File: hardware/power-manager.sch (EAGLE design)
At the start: 77 parts, among them IC1 ATMEGA168-AU, K1 G6J-2FL-Y, K2 G6J-2FL-Y, K3 G6J-2FL-Y, Q1 BSS138, Q2 BSS138, Q3 BSS138, U1 V_REG_LDOSMD, U2 INA219, U3 TPS2552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

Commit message: hw: rc2
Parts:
- added C20, C21, C22, C23: .1u, rcl:C-EUC0805
- added LED7: (no value), led:LEDSML0805
- added R24, R25, R26, R27, R28, R29: 10k, rcl:R-EU_R0603
- added R30: 330, rcl:R-EU_R0603
- added R31: 100k, rcl:R-EU_R0603
- U1: value V_REG_LDOSMD -> MIC5301
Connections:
- removed net LED_SYS: IC1.PC0(ADC0/PCINT8), R20.1
- removed net N$21: K12.P, K13.P, X2.1.SK
- new net POWER_ADC: C22.1, IC1.PC0(ADC0/PCINT8), R28.2, R29.1
- new net POWER_IN: K12.P, K13.P, R28.1, X2.1.SK
- new net USB1_ADC: C20.1, IC1.ADC7, R24.2, R25.1
- new net USB1_IN: C9.1, JP1.1, R24.1, U$2.VBUS, U3.IN
- new net USB2_ADC: C21.1, IC1.ADC6, R26.2, R27.1
- new net USB2_IN: C11.1, R26.1, U$3.VBUS, U7.IN
- net GND: now also C20.2, C21.2, C22.2, C23.2, LED7.C, R25.2, R27.2, R29.2, R31.2
- net MISO: now also R20.1
- net N$10: now also LED7.A, R30.2; no longer C11.1, U$3.VBUS, U7.IN
- net N$19: now also R31.1
- net N$5: now also C23.1, U1.BP; no longer C9.1, JP1.1, U$2.VBUS, U3.IN
- net SCK: now also R30.1
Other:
- note added: "Input Measurement"
- moved on the sheet: C1, C13, C18, C19, C2, ISP1, K1, LED1, LED2, LED3, LED4, LED5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

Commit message: hw: rc3
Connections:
- net POWER_ADC: now also IC1.ADC6; no longer IC1.PC0(ADC0/PCINT8)
- net USB1_ADC: now also IC1.PC0(ADC0/PCINT8); no longer IC1.ADC7
- net USB2_ADC: now also IC1.ADC7; no longer IC1.ADC6
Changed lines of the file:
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@@
 </segment>
 <segment>
-<pinref part="IC1" gate="1" pin="PC0(ADC0/PCINT8)"/>
-<wire x1="236.22" y1="243.84" x2="256.54" y2="243.84" width="0.1524" layer="91"/>
-<label x="256.54" y="243.84" size="1.778" layer="95" rot="MR0"/>
+<pinref part="IC1" gate="1" pin="ADC6"/>
+<wire x1="236.22" y1="228.6" x2="256.54" y2="228.6" width="0.1524" layer="91"/>
+<label x="256.54" y="228.6" size="1.778" layer="95" rot="MR0"/>
 </segment>
 </net>
@@
 </segment>
 <segment>
-<pinref part="IC1" gate="1" pin="ADC7"/>
-<wire x1="236.22" y1="226.06" x2="256.54" y2="226.06" width="0.1524" layer="91"/>
-<label x="256.54" y="226.06" size="1.778" layer="95" rot="MR0"/>
+<pinref part="IC1" gate="1" pin="PC0(ADC0/PCINT8)"/>
+<wire x1="236.22" y1="243.84" x2="256.54" y2="243.84" width="0.1524" layer="91"/>
+<label x="256.54" y="243.84" size="1.778" layer="95" rot="MR0"/>
 </segment>
 </net>
@@
 </segment>
 <segment>
-<pinref part="IC1" gate="1" pin="ADC6"/>
-<wire x1="236.22" y1="228.6" x2="256.54" y2="228.6" width="0.1524" layer="91"/>
-<label x="256.54" y="228.6" size="1.778" layer="95" rot="MR0"/>
+<pinref part="IC1" gate="1" pin="ADC7"/>
+<wire x1="236.22" y1="226.06" x2="256.54" y2="226.06" width="0.1524" layer="91"/>
+<label x="256.54" y="226.06" size="1.778" layer="95" rot="MR0"/>
 </segment>
 </net>

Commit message: hw: rc7
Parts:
- R24, R26: value 10k -> 56k
- R28: value 10k -> 270k
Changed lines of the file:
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@@
 <part name="GND48" library="supply1" deviceset="GND" device=""/>
 <part name="P+8" library="supply1" deviceset="+5V" device=""/>
-<part name="R24" library="rcl" deviceset="R-EU_" device="R0603" value="10k"/>
+<part name="R24" library="rcl" deviceset="R-EU_" device="R0603" value="56k"/>
 <part name="R25" library="rcl" deviceset="R-EU_" device="R0603" value="10k"/>
 <part name="C20" library="rcl" deviceset="C-EU" device="C0805" value=".1u"/>
 <part name="GND49" library="supply1" deviceset="GND" device=""/>
-<part name="R26" library="rcl" deviceset="R-EU_" device="R0603" value="10k"/>
+<part name="R26" library="rcl" deviceset="R-EU_" device="R0603" value="56k"/>
 <part name="R27" library="rcl" deviceset="R-EU_" device="R0603" value="10k"/>
 <part name="C21" library="rcl" deviceset="C-EU" device="C0805" value=".1u"/>
 <part name="GND50" library="supply1" deviceset="GND" device=""/>
-<part name="R28" library="rcl" deviceset="R-EU_" device="R0603" value="10k"/>
+<part name="R28" library="rcl" deviceset="R-EU_" device="R0603" value="270k"/>
 <part name="R29" library="rcl" deviceset="R-EU_" device="R0603" value="10k"/>
 <part name="C22" library="rcl" deviceset="C-EU" device="C0805" value=".1u"/>

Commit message: hw: rc8
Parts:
- R24, R26: value 56k -> 33k
- R25, R27, R29: value 10k -> 5k6
- R28: value 270k -> 180k
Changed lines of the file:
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@@
 <part name="GND48" library="supply1" deviceset="GND" device=""/>
 <part name="P+8" library="supply1" deviceset="+5V" device=""/>
-<part name="R24" library="rcl" deviceset="R-EU_" device="R0603" value="56k"/>
-<part name="R25" library="rcl" deviceset="R-EU_" device="R0603" value="10k"/>
+<part name="R24" library="rcl" deviceset="R-EU_" device="R0603" value="33k"/>
+<part name="R25" library="rcl" deviceset="R-EU_" device="R0603" value="5k6"/>
 <part name="C20" library="rcl" deviceset="C-EU" device="C0805" value=".1u"/>
 <part name="GND49" library="supply1" deviceset="GND" device=""/>
-<part name="R26" library="rcl" deviceset="R-EU_" device="R0603" value="56k"/>
-<part name="R27" library="rcl" deviceset="R-EU_" device="R0603" value="10k"/>
+<part name="R26" library="rcl" deviceset="R-EU_" device="R0603" value="33k"/>
+<part name="R27" library="rcl" deviceset="R-EU_" device="R0603" value="5k6"/>
 <part name="C21" library="rcl" deviceset="C-EU" device="C0805" value=".1u"/>
 <part name="GND50" library="supply1" deviceset="GND" device=""/>
-<part name="R28" library="rcl" deviceset="R-EU_" device="R0603" value="270k"/>
-<part name="R29" library="rcl" deviceset="R-EU_" device="R0603" value="10k"/>
+<part name="R28" library="rcl" deviceset="R-EU_" device="R0603" value="180k"/>
+<part name="R29" library="rcl" deviceset="R-EU_" device="R0603" value="5k6"/>
 <part name="C22" library="rcl" deviceset="C-EU" device="C0805" value=".1u"/>
 <part name="GND51" library="supply1" deviceset="GND" device=""/>

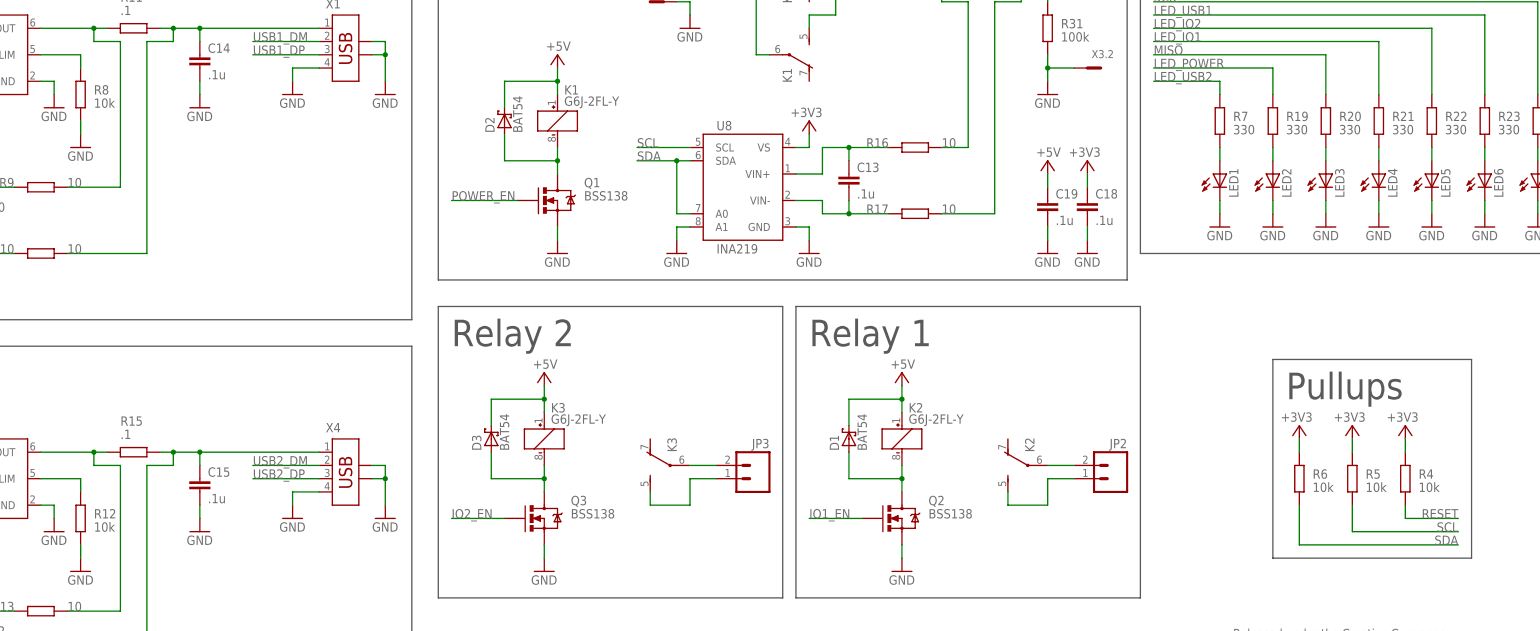
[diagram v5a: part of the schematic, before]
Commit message: hw: update part values
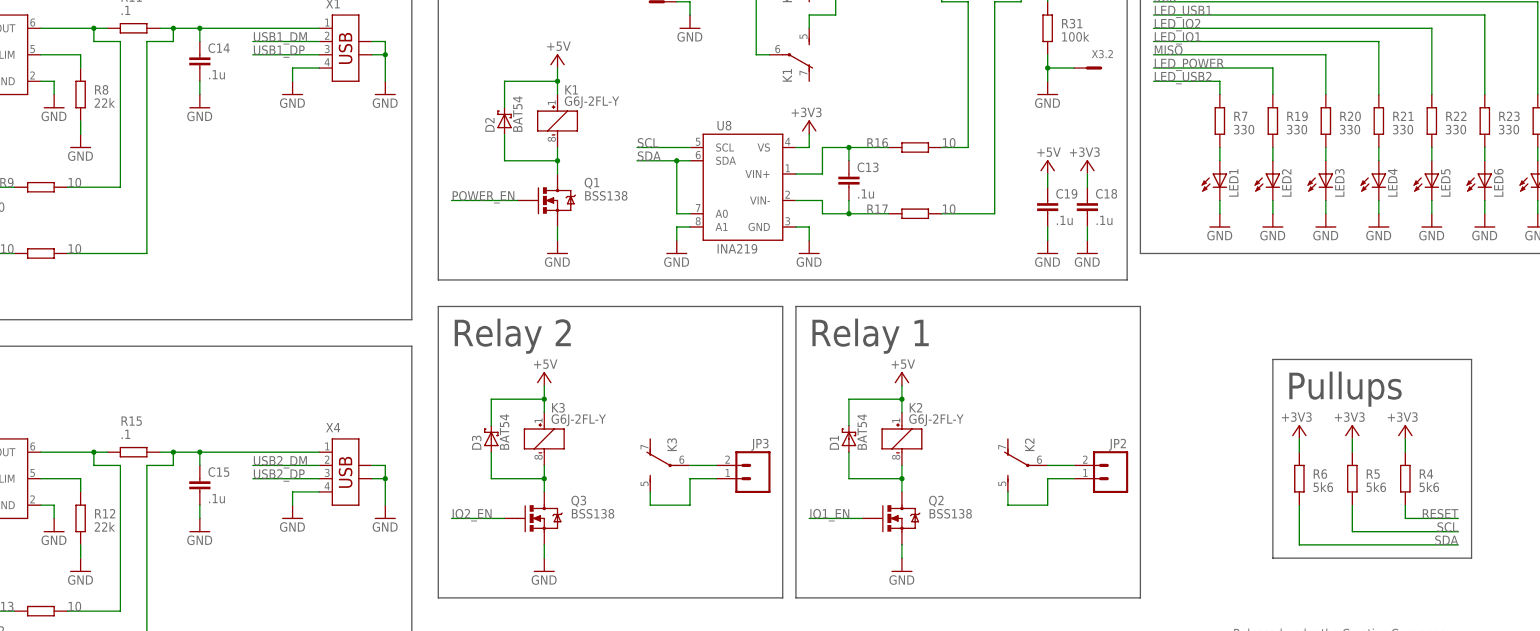
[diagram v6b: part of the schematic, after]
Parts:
- R12, R8: value 10k -> 22k
- R4, R5, R6: value 10k -> 5k6
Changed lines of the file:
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@@
 <?xml version="1.0" encoding="utf-8"?>
 <!DOCTYPE eagle SYSTEM "eagle.dtd">
-<eagle version="6.3">
+<eagle version="6.4">
 <drawing>
 <settings>
@@
 <part name="GND11" library="supply1" deviceset="GND" device=""/>
 <part name="+3V6" library="supply1" deviceset="+3V3" device=""/>
-<part name="R4" library="rcl" deviceset="R-EU_" device="R0603" value="10k"/>
+<part name="R4" library="rcl" deviceset="R-EU_" device="R0603" value="5k6"/>
 <part name="+3V7" library="supply1" deviceset="+3V3" device=""/>
-<part name="R5" library="rcl" deviceset="R-EU_" device="R0603" value="10k"/>
-<part name="R6" library="rcl" deviceset="R-EU_" device="R0603" value="10k"/>
+<part name="R5" library="rcl" deviceset="R-EU_" device="R0603" value="5k6"/>
+<part name="R6" library="rcl" deviceset="R-EU_" device="R0603" value="5k6"/>
 <part name="+3V8" library="supply1" deviceset="+3V3" device=""/>
 <part name="+3V9" library="supply1" deviceset="+3V3" device=""/>
@@
 <part name="C9" library="rcl" deviceset="C-EU" device="C0805" value=".1u"/>
 <part name="GND14" library="supply1" deviceset="GND" device=""/>
-<part name="R8" library="rcl" deviceset="R-EU_" device="R0603" value="10k"/>
+<part name="R8" library="rcl" deviceset="R-EU_" device="R0603" value="22k"/>
 <part name="GND15" library="supply1" deviceset="GND" device=""/>
 <part name="GND16" library="supply1" deviceset="GND" device=""/>
@@
 <part name="C11" library="rcl" deviceset="C-EU" device="C0805" value=".1u"/>
 <part name="GND22" library="supply1" deviceset="GND" device=""/>
-<part name="R12" library="rcl" deviceset="R-EU_" device="R0603" value="10k"/>
+<part name="R12" library="rcl" deviceset="R-EU_" device="R0603" value="22k"/>
 <part name="GND23" library="supply1" deviceset="GND" device=""/>
 <part name="GND24" library="supply1" deviceset="GND" device=""/>

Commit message: hw: add notes and pdf
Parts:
- K1, K2, K3: value G6J-2FL-Y -> IM03GR
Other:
- note added: "<-- GREEN"
- note added: "RED"
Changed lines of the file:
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@@
 <part name="JP1" library="SparkFun-Connectors" deviceset="M02" device="PTH"/>
 <part name="U2" library="balto" deviceset="INA219" device=""/>
-<part name="K1" library="relay" deviceset="G6J*-2?-Y" device="FL"/>
+<part name="K1" library="relay" deviceset="G6J*-2?-Y" device="FL" value="IM03GR"/>
 <part name="U3" library="balto" deviceset="TPS2552" device=""/>
 <part name="P+2" library="supply1" deviceset="+5V" device=""/>
@@
 <part name="GND36" library="supply1" deviceset="GND" device=""/>
 <part name="D1" library="diode" deviceset="BAT54" device=""/>
-<part name="K2" library="relay" deviceset="G6J*-2?-Y" device="FL"/>
+<part name="K2" library="relay" deviceset="G6J*-2?-Y" device="FL" value="IM03GR"/>
 <part name="P+6" library="supply1" deviceset="+5V" device=""/>
 <part name="Q2" library="SparkFun-DiscreteSemi" deviceset="BSS138" device="TRANS-00830" value="BSS138"/>
@@
 <part name="JP2" library="SparkFun-Connectors" deviceset="M02" device="PTH"/>
 <part name="D3" library="diode" deviceset="BAT54" device=""/>
-<part name="K3" library="relay" deviceset="G6J*-2?-Y" device="FL"/>
+<part name="K3" library="relay" deviceset="G6J*-2?-Y" device="FL" value="IM03GR"/>
 <part name="P+7" library="supply1" deviceset="+5V" device=""/>
 <part name="Q3" library="SparkFun-DiscreteSemi" deviceset="BSS138" device="TRANS-00830" value="BSS138"/>
@@
 <wire x1="363.22" y1="48.26" x2="325.12" y2="48.26" width="0.1524" layer="97"/>
 <wire x1="325.12" y1="48.26" x2="325.12" y2="86.36" width="0.1524" layer="97"/>
-<wire x1="299.72" y1="106.68" x2="383.54" y2="106.68" width="0.1524" layer="97"/>
-<wire x1="383.54" y1="106.68" x2="383.54" y2="170.18" width="0.1524" layer="97"/>
-<wire x1="383.54" y1="170.18" x2="299.72" y2="170.18" width="0.1524" layer="97"/>
-<wire x1="299.72" y1="170.18" x2="299.72" y2="106.68" width="0.1524" layer="97"/>
+<wire x1="299.72" y1="104.14" x2="386.08" y2="104.14" width="0.1524" layer="97"/>
+<wire x1="386.08" y1="104.14" x2="386.08" y2="170.18" width="0.1524" layer="97"/>
+<wire x1="386.08" y1="170.18" x2="299.72" y2="170.18" width="0.1524" layer="97"/>
+<wire x1="299.72" y1="170.18" x2="299.72" y2="104.14" width="0.1524" layer="97"/>
 <wire x1="5.08" y1="170.18" x2="160.02" y2="170.18" width="0.1524" layer="97"/>
 <wire x1="160.02" y1="170.18" x2="160.02" y2="93.98" width="0.1524" layer="97"/>
@@
 <wire x1="363.22" y1="175.26" x2="264.16" y2="175.26" width="0.1524" layer="97"/>
 <wire x1="264.16" y1="175.26" x2="264.16" y2="228.6" width="0.1524" layer="97"/>
+<text x="373.38" y="106.68" size="1.778" layer="97">RED</text>
+<text x="355.6" y="106.68" size="1.778" layer="97">&lt;-- GREEN</text>
 </plain>
 <instances>

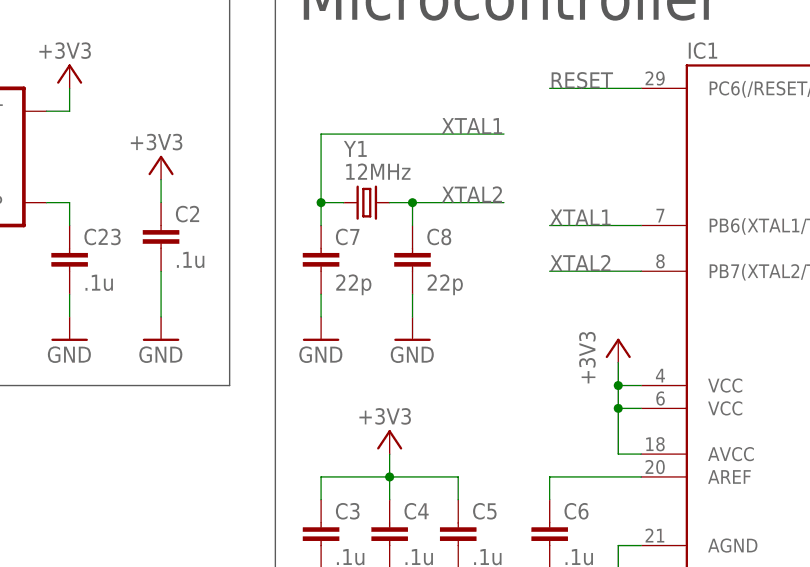
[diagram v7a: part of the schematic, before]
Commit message: hw: update xtal cap values to 33p
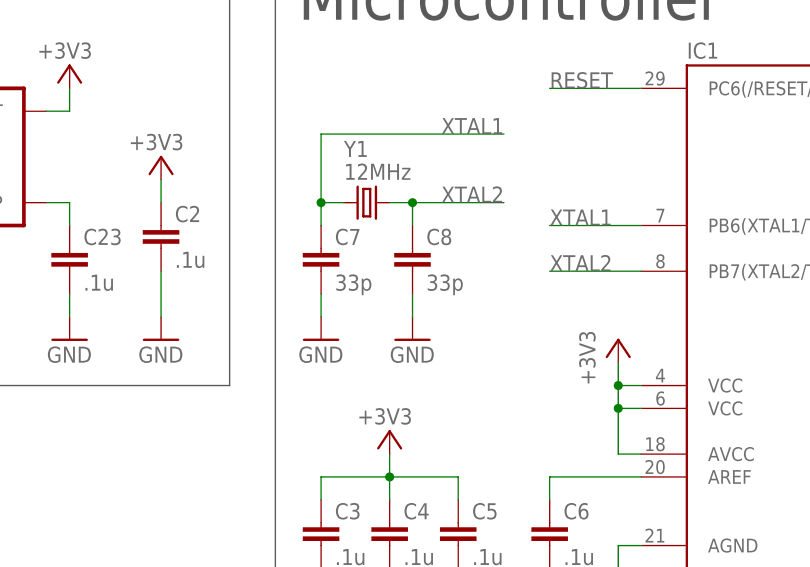
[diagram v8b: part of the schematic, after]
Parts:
- C7, C8: value 22p -> 33p
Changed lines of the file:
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@@
 <part name="+3V5" library="supply1" deviceset="+3V3" device=""/>
 <part name="Y1" library="SparkFun-FreqCtrl" deviceset="CRYSTAL" device="5X3" value="12MHz"/>
-<part name="C7" library="rcl" deviceset="C-EU" device="C0805" value="22p"/>
-<part name="C8" library="rcl" deviceset="C-EU" device="C0805" value="22p"/>
+<part name="C7" library="rcl" deviceset="C-EU" device="C0805" value="33p"/>
+<part name="C8" library="rcl" deviceset="C-EU" device="C0805" value="33p"/>
 <part name="GND9" library="supply1" deviceset="GND" device=""/>
 <part name="GND10" library="supply1" deviceset="GND" device=""/>
